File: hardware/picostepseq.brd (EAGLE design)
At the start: 125.7 x 54.6 mm, 27 parts, among them J1 SJ-3523-SMT, J2 SJ-3523-SMT, SW1 LED_SWITCHSTEP, SW2 LED_SWITCHSTEP, SW3 LED_SWITCHSTEP, SW4 LED_SWITCHSTEP, SW5 LED_SWITCHSTEP, SW6 LED_SWITCHSTEP, SW7 LED_SWITCHSTEP, SW8 LED_SWITCHSTEP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

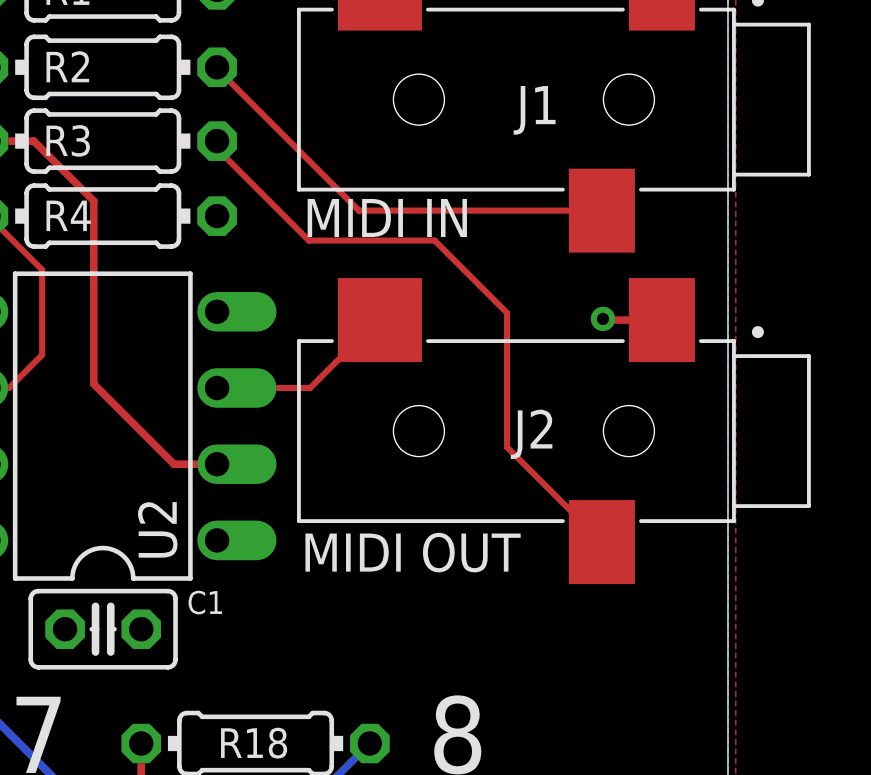
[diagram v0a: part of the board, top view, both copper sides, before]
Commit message: move MIDI IN and MIDI OUT labels because I am dumb
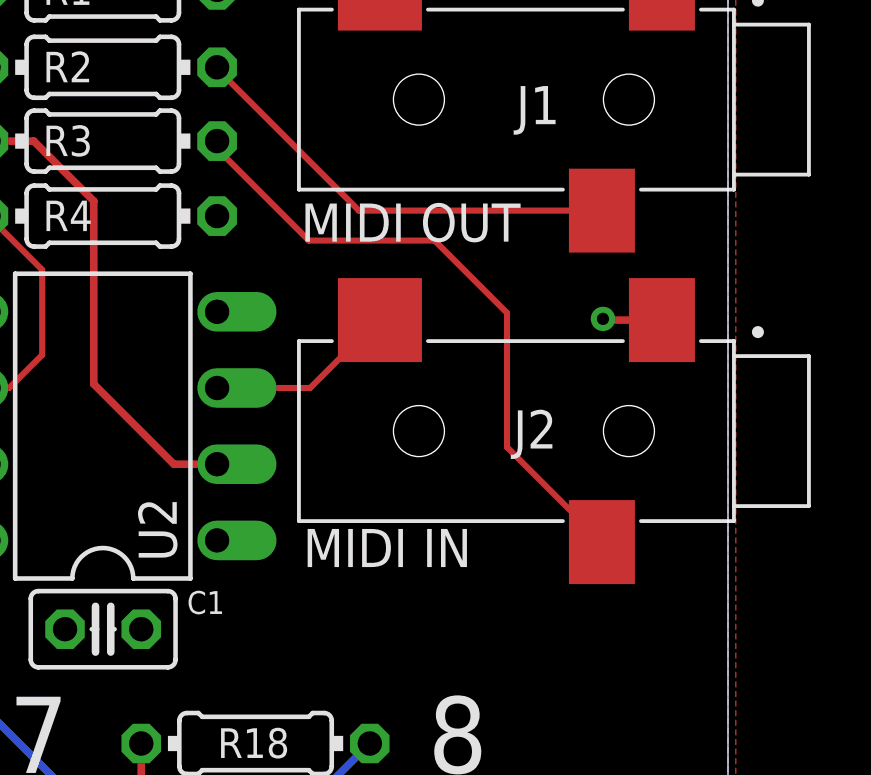
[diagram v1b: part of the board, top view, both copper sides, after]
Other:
- board text added: "picostepseq_7Aug2022"
- board text removed: "picostepseq_4Aug2022"
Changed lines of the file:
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@@
 <grid distance="0.5" unitdist="mm" unit="mm" style="lines" multiple="1" display="no" altdistance="1" altunitdist="mm" altunit="mm"/>
 <layers>
-<layer number="1" name="Top" color="4" fill="1" visible="no" active="yes"/>
+<layer number="1" name="Top" color="4" fill="1" visible="yes" active="yes"/>
 <layer number="2" name="Route2" color="16" fill="1" visible="no" active="no"/>
 <layer number="3" name="Route3" color="17" fill="1" visible="no" active="no"/>
@@
 <layer number="19" name="Unrouted" color="6" fill="1" visible="yes" active="yes"/>
 <layer number="20" name="Dimension" color="15" fill="1" visible="yes" active="yes"/>
-<layer number="21" name="tPlace" color="7" fill="1" visible="no" active="yes"/>
+<layer number="21" name="tPlace" color="7" fill="1" visible="yes" active="yes"/>
 <layer number="22" name="bPlace" color="7" fill="1" visible="yes" active="yes"/>
-<layer number="23" name="tOrigins" color="15" fill="1" visible="no" active="yes"/>
+<layer number="23" name="tOrigins" color="15" fill="1" visible="yes" active="yes"/>
 <layer number="24" name="bOrigins" color="15" fill="1" visible="yes" active="yes"/>
-<layer number="25" name="tNames" color="7" fill="1" visible="no" active="yes"/>
+<layer number="25" name="tNames" color="7" fill="1" visible="yes" active="yes"/>
 <layer number="26" name="bNames" color="7" fill="1" visible="yes" active="yes"/>
 <layer number="27" name="tValues" color="7" fill="1" visible="no" active="yes"/>
@@
 <layer number="37" name="tTest" color="7" fill="1" visible="no" active="yes"/>
 <layer number="38" name="bTest" color="7" fill="1" visible="no" active="yes"/>
-<layer number="39" name="tKeepout" color="4" fill="11" visible="no" active="yes"/>
+<layer number="39" name="tKeepout" color="4" fill="11" visible="yes" active="yes"/>
 <layer number="40" name="bKeepout" color="1" fill="11" visible="yes" active="yes"/>
-<layer number="41" name="tRestrict" color="4" fill="10" visible="no" active="yes"/>
+<layer number="41" name="tRestrict" color="4" fill="10" visible="yes" active="yes"/>
 <layer number="42" name="bRestrict" color="1" fill="10" visible="yes" active="yes"/>
 <layer number="43" name="vRestrict" color="2" fill="10" visible="no" active="yes"/>
@@
 <layer number="49" name="Reference" color="7" fill="1" visible="no" active="yes"/>
 <layer number="50" name="dxf" color="7" fill="1" visible="no" active="no"/>
-<layer number="51" name="tDocu" color="7" fill="1" visible="no" active="yes"/>
+<layer number="51" name="tDocu" color="7" fill="1" visible="yes" active="yes"/>
 <layer number="52" name="bDocu" color="7" fill="1" visible="yes" active="yes"/>
 <layer number="53" name="tGND_GNDA" color="7" fill="9" visible="no" active="no"/>
@@
 <wire x1="123.19" y1="54.61" x2="2.54" y2="54.61" width="0" layer="20"/>
 <wire x1="2.54" y1="54.61" x2="0" y2="52.07" width="0" layer="20" curve="90"/>
-<text x="38.7835" y="42.1695" size="0.9" layer="22" font="vector" ratio="10" rot="MR0">picostepseq_4Aug2022</text>
-<text x="111.4915" y="28.5895" size="1.27" layer="21" font="vector" ratio="14">MIDI OUT</text>
-<text x="111.5645" y="39.7415" size="1.27" layer="21" font="vector" ratio="14">MIDI IN</text>
+<text x="38.7835" y="42.1695" size="0.9" layer="22" font="vector" ratio="10" rot="MR0">picostepseq_7Aug2022</text>
+<text x="111.4915" y="39.5895" size="1.27" layer="21" font="vector" ratio="14">MIDI OUT</text>
+<text x="111.5645" y="28.7415" size="1.27" layer="21" font="vector" ratio="14">MIDI IN</text>
 <text x="120.5" y="39" size="1.778" layer="22" rot="SMR270" align="bottom-center">MIDI
 TRS-A</text>
-<text x="120" y="47.5" size="1.778" layer="22" rot="SMR270" align="bottom-center">IN</text>
-<text x="120.38" y="30.25" size="1.778" layer="22" rot="SMR270" align="bottom-center">OUT</text>
+<text x="120" y="30" size="1.778" layer="22" rot="SMR270" align="bottom-center">IN</text>
+<text x="120.38" y="47.25" size="1.778" layer="22" rot="SMR270" align="bottom-center">OUT</text>
 <text x="77.47" y="40.64" size="1.778" layer="22" rot="SMR0">Pico Step Seq</text>
 <text x="38.7675" y="44.3865" size="0.9" layer="22" font="vector" ratio="10" rot="MR0">github.com/todbot/picostepseq</text>
